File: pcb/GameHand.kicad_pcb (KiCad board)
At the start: 2 copper layers, 142.5 x 111.3 mm, 75 parts, among them J1 USB_C_Receptacle_USB2.0, U1 ATmega32U2-AU, U2 SRV05-4, X1 Crystal_GND24_Small

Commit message: update gerbers
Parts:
- removed REF**: OSHW-Logo_7.5x8mm_SilkScreen, Symbol:OSHW-Logo_7.5x8mm_SilkScreen

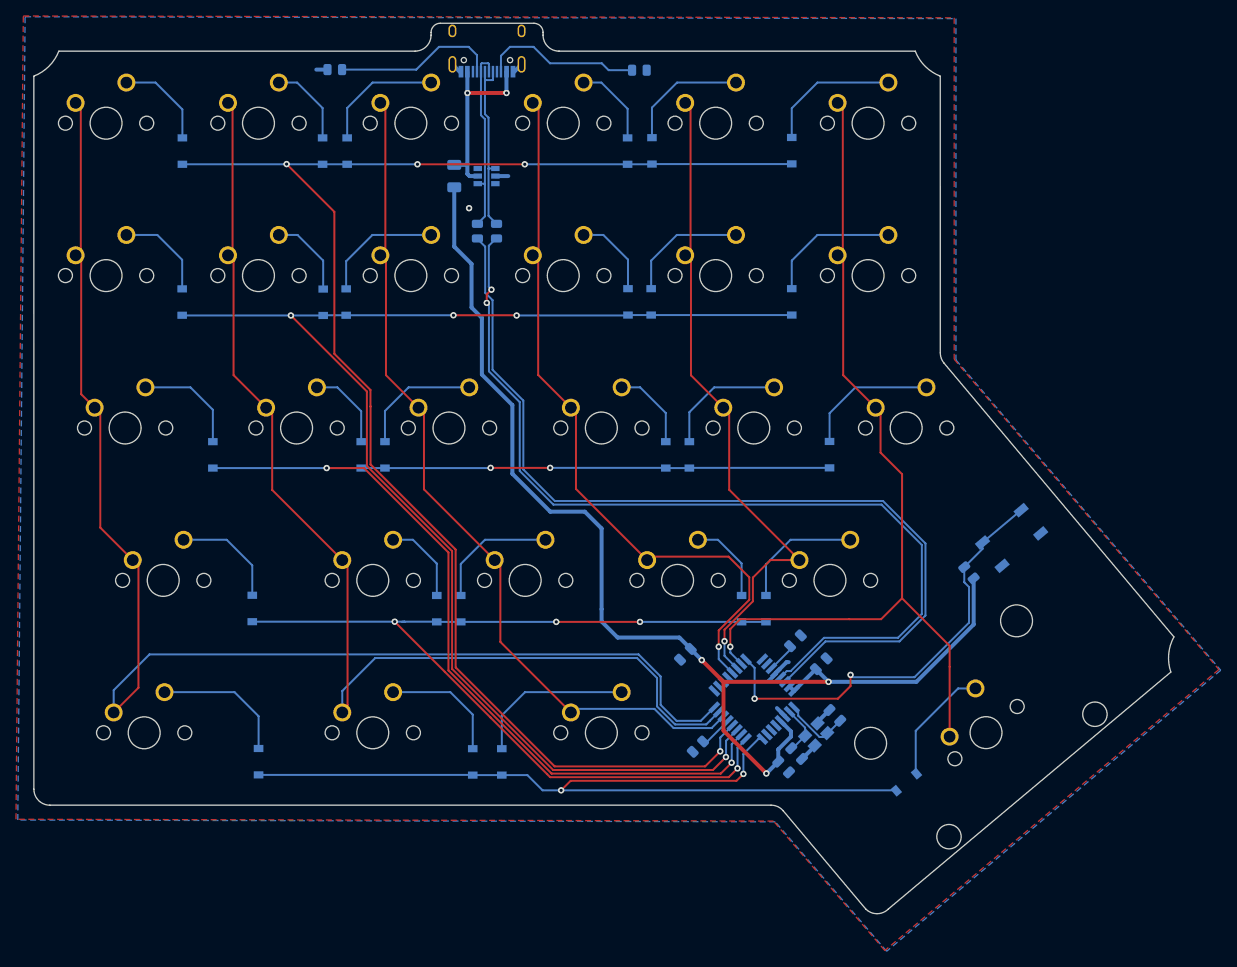
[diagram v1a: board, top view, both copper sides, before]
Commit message: remove unused corner cutouts
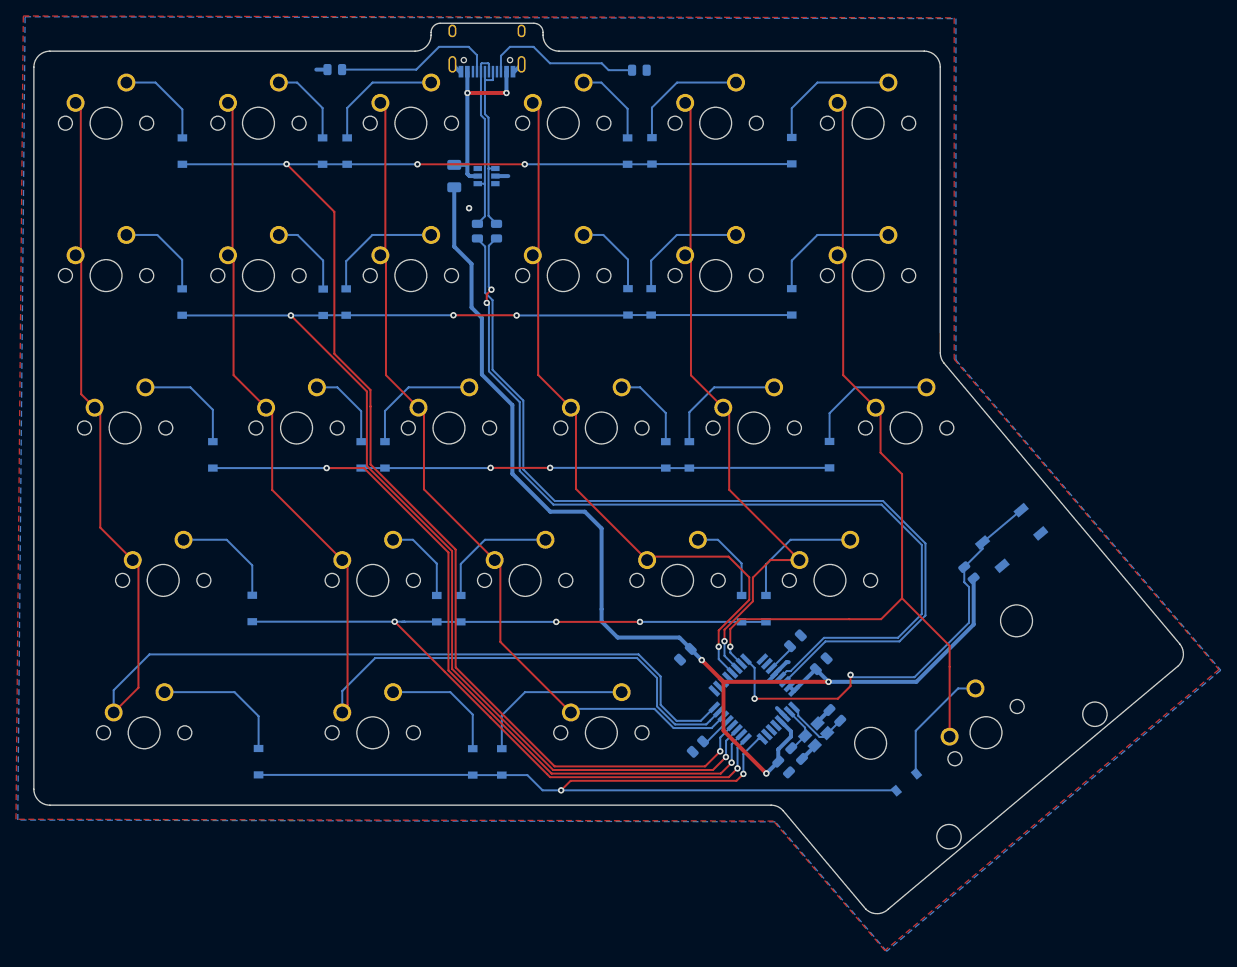
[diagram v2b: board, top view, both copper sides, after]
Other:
- board size 142.5 x 111.3 mm -> 143.7 x 111.3 mm
